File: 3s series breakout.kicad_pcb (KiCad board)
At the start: 2 copper layers, 34 x 80 mm, 14 parts, among them M1 MountingHole_2.2mm_M2_Pad_Via, M2 MountingHole_2.2mm_M2_Pad_Via, M3 MountingHole_2.2mm_M2_Pad_Via

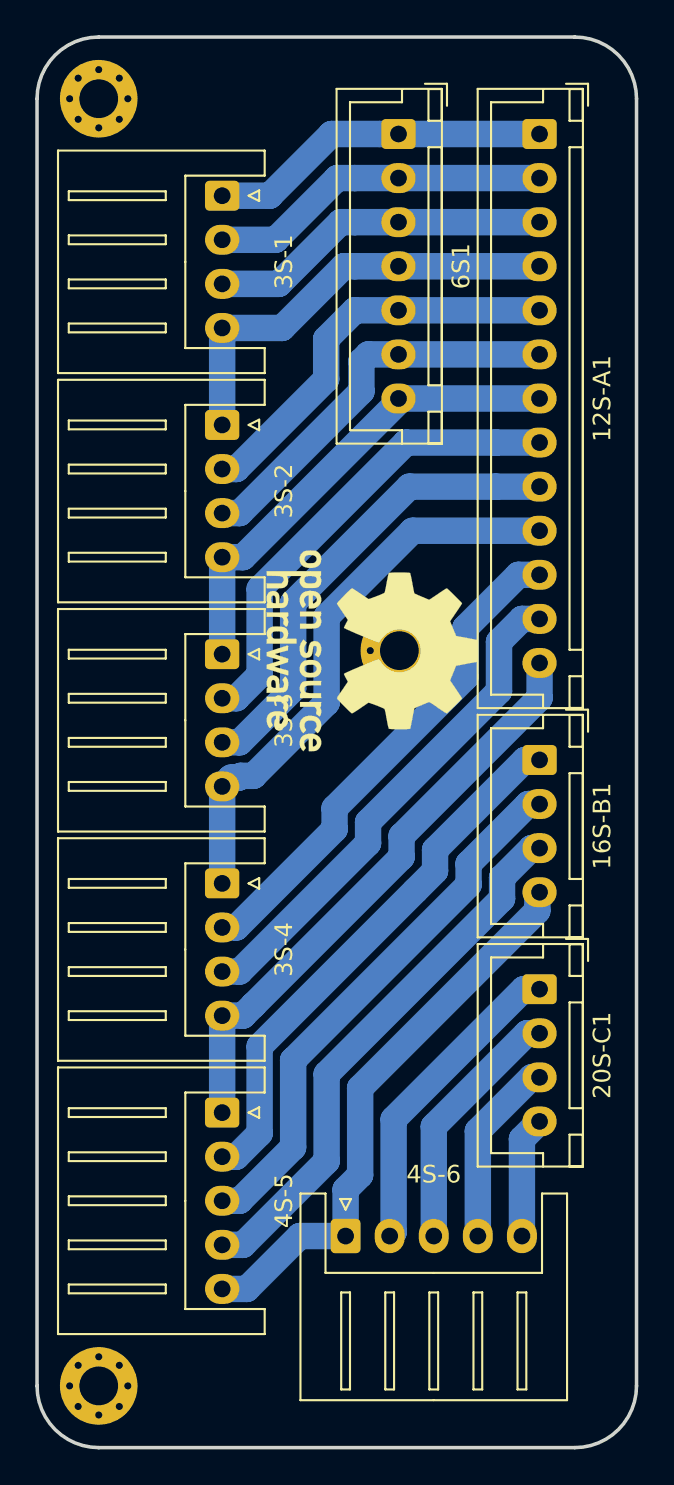
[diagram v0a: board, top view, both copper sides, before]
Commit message: add logos and fix up most labels
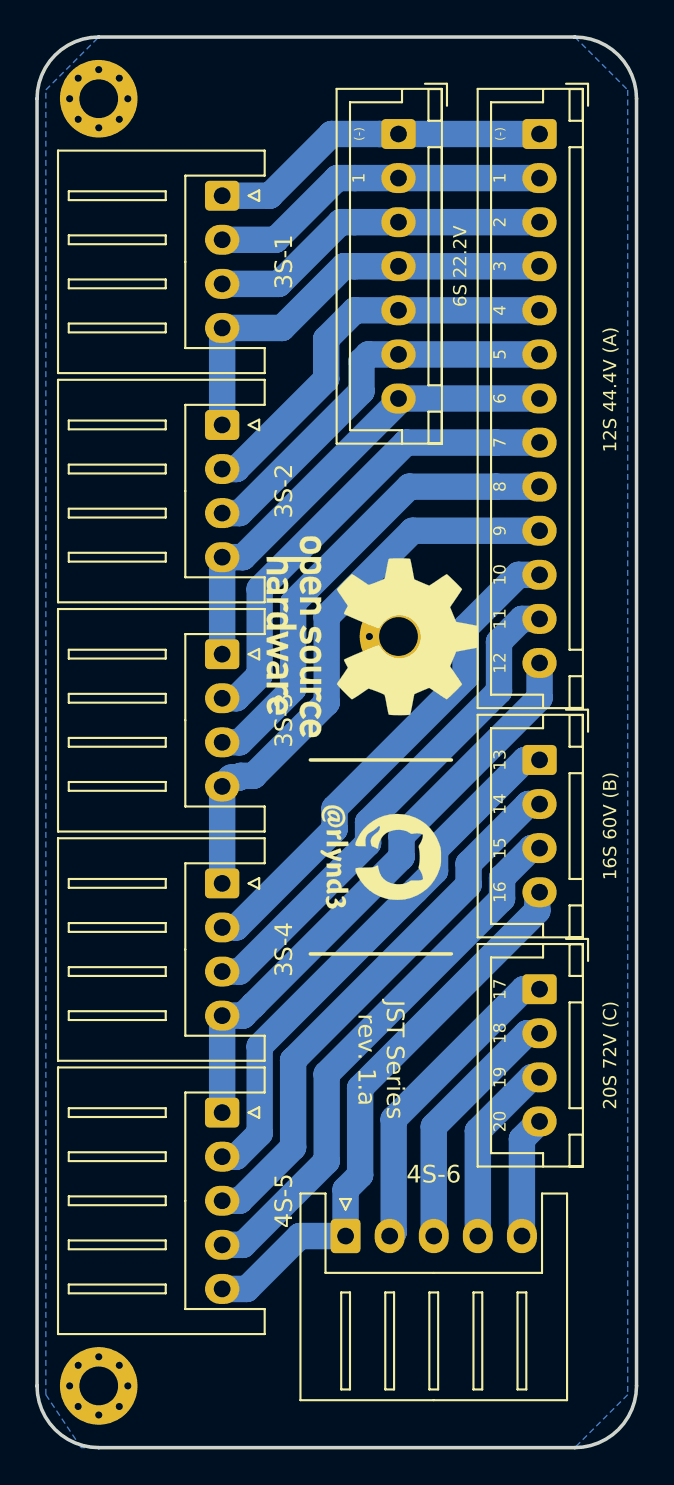
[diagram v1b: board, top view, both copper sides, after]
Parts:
- added G***: LOGO, Github_rlynd3:github-rlynd_6mm, F.Cu at (143.0, 81.5)
- moved M2 0.80 mm to (144.0, 69.0)
- moved REF** 0.80 mm to (142.5, 69.0)
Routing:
- added copper zone on B.Cu, net (none)
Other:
- board text added: "(-)"
- board text added: "1"
- board text added: "10"
- board text added: "11"
- board text added: "12"
- board text added: "12S 44.4V (A)"
- board text added: "13"
- board text added: "14"
- board text added: "15"
- board text added: "16"
- board text added: "16S 60V (B)"
- board text added: "17"
- board text added: "18"
- board text added: "19"
- board text added: "2"
- board text added: "20"
- board text added: "20S 72V (C)"
- board text added: "3"
- board text added: "4"
- board text added: "5"
- board text added: "6"
- board text added: "6S 22.2V"
- board text added: "7"
- board text added: "8"
- board text added: "9"
- board text added: "JST Series rev. 1.a"

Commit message: clean up labels
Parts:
- REF**: value OSHW-Logo_11.4x12mm_SilkScreen -> OSHW-Logo2_9.8x8mm_SilkScreen; footprint Symbol:OSHW-Logo_11.4x12mm_SilkScreen -> Symbol:OSHW-Logo2_9.8x8mm_SilkScreen
- moved REF** 0.90 mm to (143.4, 69.0)
- moved G*** 0.10 mm to (143.1, 81.5)
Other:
- board text removed: "(-)"

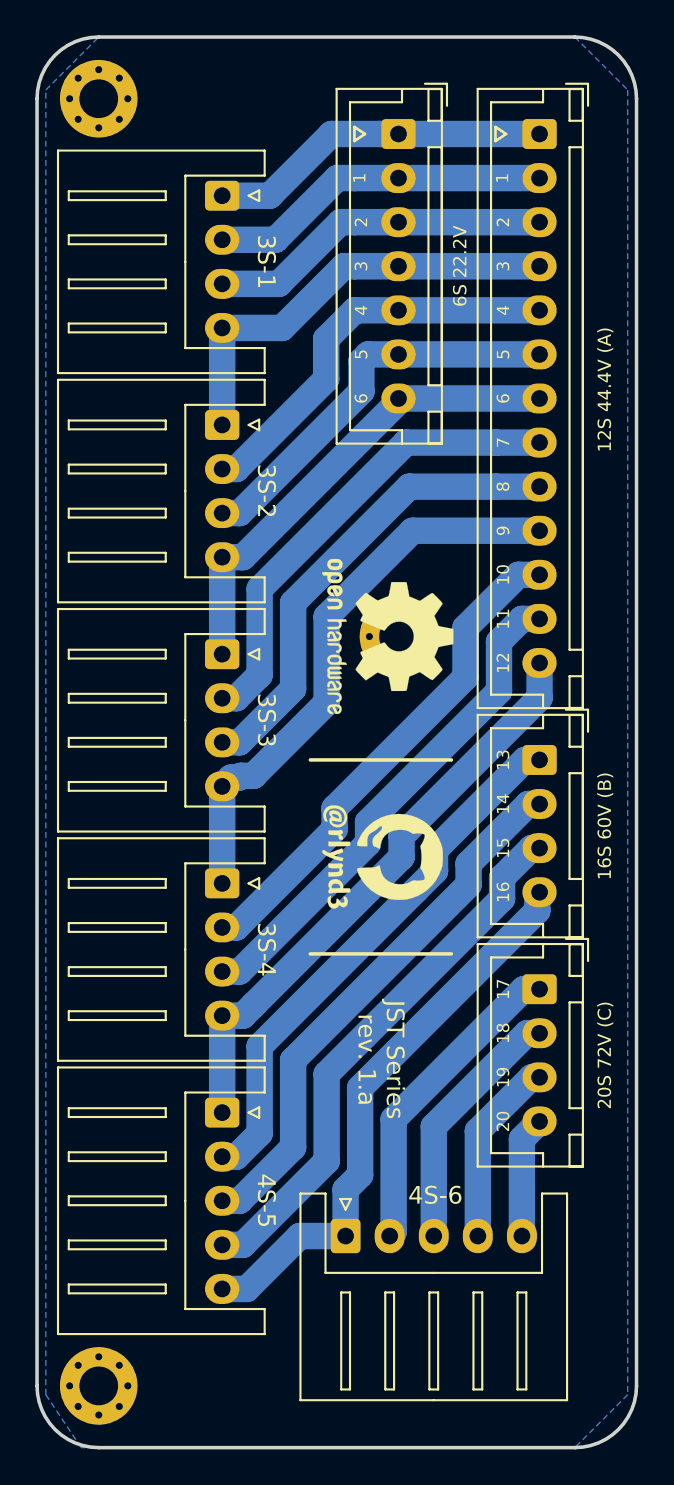
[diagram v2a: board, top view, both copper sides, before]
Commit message: add images and clean-up labels
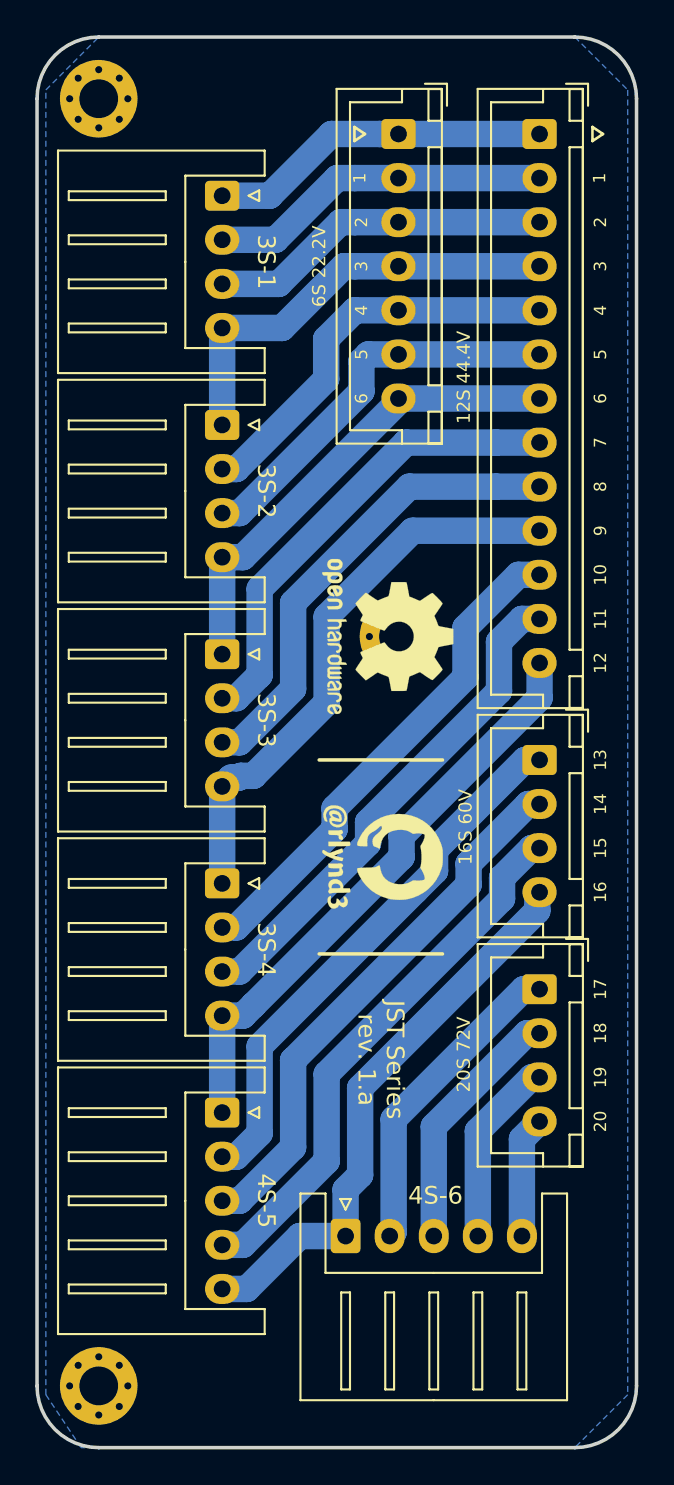
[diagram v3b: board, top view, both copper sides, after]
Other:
- board text added: "12S 44.4V"
- board text added: "16S 60V"
- board text added: "20S 72V"
- board text removed: "12S 44.4V (A)"
- board text removed: "16S 60V (B)"
- board text removed: "20S 72V (C)"
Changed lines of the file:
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@@
   (page A4)
   (layers
-    (0 F.Cu signal hide)
-    (31 B.Cu signal)
+    (0 F.Cu signal)
+    (31 B.Cu signal hide)
     (32 B.Adhes user hide)
     (33 F.Adhes user hide)
@@
     (descr "JST XH series connector, B04B-XH-A (http://www.jst-mfg.com/product/pdf/eng/eXH.pdf), generated with kicad-footprint-generator")
     (tags "connector JST XH side entry")
-    (fp_text reference 20S-C1 (at 3.75 4.25 270) (layer F.SilkS) hide
+    (fp_text reference 20S-C1 (at 3.75 2 270) (layer F.SilkS) hide
       (effects (font (size 1 1) (thickness 0.15)))
     )
@@
     (descr "JST XH series connector, B13B-XH-A (http://www.jst-mfg.com/product/pdf/eng/eXH.pdf), generated with kicad-footprint-generator")
     (tags "connector JST XH side entry")
-    (fp_text reference 12S-A1 (at 15 4.25 270) (layer F.SilkS) hide
+    (fp_text reference 12S-A1 (at 15 2 270) (layer F.SilkS) hide
       (effects (font (size 1 1) (thickness 0.15)))
     )
@@
     (descr "JST XH series connector, B04B-XH-A (http://www.jst-mfg.com/product/pdf/eng/eXH.pdf), generated with kicad-footprint-generator")
     (tags "connector JST XH side entry")
-    (fp_text reference 16S-B1 (at 3.75 4.25 270) (layer F.SilkS) hide
+    (fp_text reference 16S-B1 (at 3.5 2 270) (layer F.SilkS) hide
       (effects (font (size 1 1) (thickness 0.15)))
     )
@@
     (descr "JST XH series connector, B07B-XH-A (http://www.jst-mfg.com/product/pdf/eng/eXH.pdf), generated with kicad-footprint-generator")
     (tags "connector JST XH side entry")
-    (fp_text reference 6S1 (at 7.5 4 270) (layer F.SilkS) hide
+    (fp_text reference 6S1 (at 7.5 0 270) (layer F.SilkS) hide
       (effects (font (size 1 1) (thickness 0.15)))
     )
@@
   (gr_line (start 141.5 40.9) (end 142.1 40.5) (layer F.SilkS) (width 0.15))
   (gr_line (start 141.5 40.1) (end 141.5 40.9) (layer F.SilkS) (width 0.15))
-  (gr_line (start 150.1 40.5) (end 149.5 40.1) (layer F.SilkS) (width 0.15))
-  (gr_line (start 149.5 40.9) (end 150.1 40.5) (layer F.SilkS) (width 0.15))
-  (gr_line (start 149.5 40.1) (end 149.5 40.9) (layer F.SilkS) (width 0.15))
-  (gr_text 20 (at 149.95 96.5 90) (layer F.SilkS)
-    (effects (font (size 0.7 0.7) (thickness 0.15)))
-  )
-  (gr_text 19 (at 149.95 94 90) (layer F.SilkS)
-    (effects (font (size 0.7 0.7) (thickness 0.15)))
-  )
-  (gr_text 18 (at 149.95 91.5 90) (layer F.SilkS)
-    (effects (font (size 0.7 0.7) (thickness 0.15)))
-  )
-  (gr_text 17 (at 149.95 89 90) (layer F.SilkS)
-    (effects (font (size 0.7 0.7) (thickness 0.15)))
-  )
-  (gr_text 16 (at 149.95 83.5 90) (layer F.SilkS)
-    (effects (font (size 0.7 0.7) (thickness 0.15)))
-  )
-  (gr_text 15 (at 149.95 81 90) (layer F.SilkS)
-    (effects (font (size 0.7 0.7) (thickness 0.15)))
-  )
-  (gr_text 14 (at 149.95 78.5 90) (layer F.SilkS)
-    (effects (font (size 0.7 0.7) (thickness 0.15)))
-  )
-  (gr_text 13 (at 149.95 76 90) (layer F.SilkS)
-    (effects (font (size 0.7 0.7) (thickness 0.15)))
-  )
-  (gr_text 12 (at 149.95 70.5 90) (layer F.SilkS)
-    (effects (font (size 0.7 0.7) (thickness 0.15)))
-  )
-  (gr_text 11 (at 149.95 68 90) (layer F.SilkS)
-    (effects (font (size 0.7 0.7) (thickness 0.15)))
-  )
-  (gr_text 10 (at 149.95 65.5 90) (layer F.SilkS)
-    (effects (font (size 0.7 0.7) (thickness 0.15)))
-  )
-  (gr_text 9 (at 149.95 63 90) (layer F.SilkS)
-    (effects (font (size 0.7 0.7) (thickness 0.15)))
-  )
-  (gr_text 8 (at 149.95 60.5 90) (layer F.SilkS)
-    (effects (font (size 0.7 0.7) (thickness 0.15)))
-  )
-  (gr_text 7 (at 149.95 58 90) (layer F.SilkS)
-    (effects (font (size 0.7 0.7) (thickness 0.15)))
-  )
-  (gr_text 6 (at 149.95 55.5 90) (layer F.SilkS)
-    (effects (font (size 0.7 0.7) (thickness 0.15)))
-  )
-  (gr_text 5 (at 149.95 53 90) (layer F.SilkS)
-    (effects (font (size 0.7 0.7) (thickness 0.15)))
-  )
-  (gr_text 4 (at 149.95 50.5 90) (layer F.SilkS)
-    (effects (font (size 0.7 0.7) (thickness 0.15)))
-  )
-  (gr_text 3 (at 149.95 48 90) (layer F.SilkS)
-    (effects (font (size 0.7 0.7) (thickness 0.15)))
-  )
-  (gr_text 2 (at 149.95 45.5 90) (layer F.SilkS)
-    (effects (font (size 0.7 0.7) (thickness 0.15)))
-  )
-  (gr_text 1 (at 149.9 43 90) (layer F.SilkS)
+  (gr_line (start 155.6 40.5) (end 155 40.1) (layer F.SilkS) (width 0.15))
+  (gr_line (start 155 40.9) (end 155.6 40.5) (layer F.SilkS) (width 0.15))
+  (gr_line (start 155 40.1) (end 155 40.9) (layer F.SilkS) (width 0.15))
+  (gr_text 20 (at 155.45 96.5 90) (layer F.SilkS)
+    (effects (font (size 0.7 0.7) (thickness 0.15)))
+  )
+  (gr_text 19 (at 155.45 94 90) (layer F.SilkS)
+    (effects (font (size 0.7 0.7) (thickness 0.15)))
+  )
+  (gr_text 18 (at 155.45 91.5 90) (layer F.SilkS)
+    (effects (font (size 0.7 0.7) (thickness 0.15)))
+  )
+  (gr_text 17 (at 155.45 89 90) (layer F.SilkS)
+    (effects (font (size 0.7 0.7) (thickness 0.15)))
+  )
+  (gr_text 16 (at 155.45 83.5 90) (layer F.SilkS)
+    (effects (font (size 0.7 0.7) (thickness 0.15)))
+  )
+  (gr_text 15 (at 155.45 81 90) (layer F.SilkS)
+    (effects (font (size 0.7 0.7) (thickness 0.15)))
+  )
+  (gr_text 14 (at 155.45 78.5 90) (layer F.SilkS)
+    (effects (font (size 0.7 0.7) (thickness 0.15)))
+  )
+  (gr_text 13 (at 155.45 76 90) (layer F.SilkS)
+    (effects (font (size 0.7 0.7) (thickness 0.15)))
+  )
+  (gr_text 12 (at 155.45 70.5 90) (layer F.SilkS)
+    (effects (font (size 0.7 0.7) (thickness 0.15)))
+  )
+  (gr_text 11 (at 155.45 68 90) (layer F.SilkS)
+    (effects (font (size 0.7 0.7) (thickness 0.15)))
+  )
+  (gr_text 10 (at 155.45 65.5 90) (layer F.SilkS)
+    (effects (font (size 0.7 0.7) (thickness 0.15)))
+  )
+  (gr_text 9 (at 155.45 63 90) (layer F.SilkS)
+    (effects (font (size 0.7 0.7) (thickness 0.15)))
+  )
+  (gr_text 8 (at 155.45 60.5 90) (layer F.SilkS)
+    (effects (font (size 0.7 0.7) (thickness 0.15)))
+  )
+  (gr_text 7 (at 155.45 58 90) (layer F.SilkS)
+    (effects (font (size 0.7 0.7) (thickness 0.15)))
+  )
+  (gr_text 6 (at 155.45 55.5 90) (layer F.SilkS)
+    (effects (font (size 0.7 0.7) (thickness 0.15)))
+  )
+  (gr_text 5 (at 155.45 53 90) (layer F.SilkS)
+    (effects (font (size 0.7 0.7) (thickness 0.15)))
+  )
+  (gr_text 4 (at 155.45 50.5 90) (layer F.SilkS)
+    (effects (font (size 0.7 0.7) (thickness 0.15)))
+  )
+  (gr_text 3 (at 155.45 48 90) (layer F.SilkS)
+    (effects (font (size 0.7 0.7) (thickness 0.15)))
+  )
+  (gr_text 2 (at 155.45 45.5 90) (layer F.SilkS)
+    (effects (font (size 0.7 0.7) (thickness 0.15)))
+  )
+  (gr_text 1 (at 155.4 43 90) (layer F.SilkS)
     (effects (font (size 0.7 0.7) (thickness 0.15)))
   )
@@
     (effects (font (size 0.7 0.7) (thickness 0.15)))
   )
-  (gr_text "6S 22.2V" (at 147.5 48 90) (layer F.SilkS)
+  (gr_text "6S 22.2V" (at 139.5 48 90) (layer F.SilkS)
     (effects (font (size 0.75 0.75) (thickness 0.15)))
   )
-  (gr_text "16S 60V (B)" (at 155.7 79.75 90) (layer F.SilkS)
+  (gr_text "16S 60V" (at 147.8 79.8 90) (layer F.SilkS)
     (effects (font (size 0.75 0.75) (thickness 0.15)))
   )
-  (gr_text "20S 72V (C)" (at 155.7 92.75 90) (layer F.SilkS)
+  (gr_text "20S 72V" (at 147.7 92.7 90) (layer F.SilkS)
     (effects (font (size 0.75 0.75) (thickness 0.15)))
   )
-  (gr_text "12S 44.4V (A)" (at 155.7 55 90) (layer F.SilkS)
+  (gr_text "12S 44.4V" (at 147.7 54.3 90) (layer F.SilkS)
     (effects (font (size 0.75 0.75) (thickness 0.15)))
   )
-  (gr_line (start 147 87) (end 139 87) (layer F.SilkS) (width 0.2))
+  (gr_line (start 146.5 87) (end 139.5 87) (layer F.SilkS) (width 0.2))
   (gr_text "JST Series\nrev. 1.a" (at 143 93 270) (layer F.SilkS)
     (effects (font (size 1 1) (thickness 0.25)))
   )
-  (gr_line (start 147 76) (end 139 76) (layer F.SilkS) (width 0.2))
+  (gr_line (start 146.5 76) (end 139.5 76) (layer F.SilkS) (width 0.2))
   (gr_arc (start 127 111.5) (end 123.5 111.5) (angle -90) (layer Edge.Cuts) (width 0.2))
   (gr_arc (start 154 111.5) (end 154 115) (angle -90) (layer Edge.Cuts) (width 0.2))
